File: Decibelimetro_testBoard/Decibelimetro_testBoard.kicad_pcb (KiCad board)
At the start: 2 copper layers, 80 x 65 mm, 16 parts, among them J1 Conn_01x02_Pin, SW1 SW_Push, SW2 SW_Push, U1 ESP32-DEVKITV1-30PIN, U2 INMP441, U3 TFT 1.44" ST7735

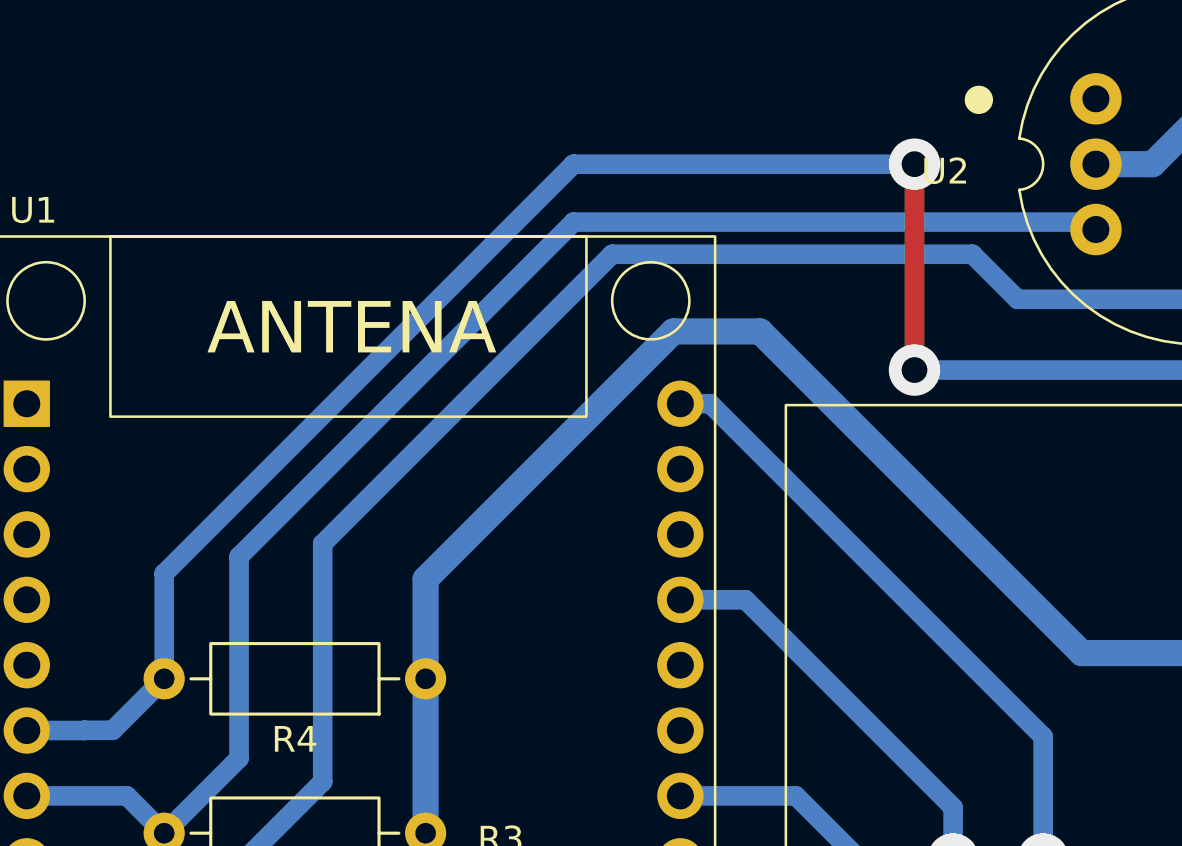
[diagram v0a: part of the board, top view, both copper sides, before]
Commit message: Incorporo cambios de código sonometroV2
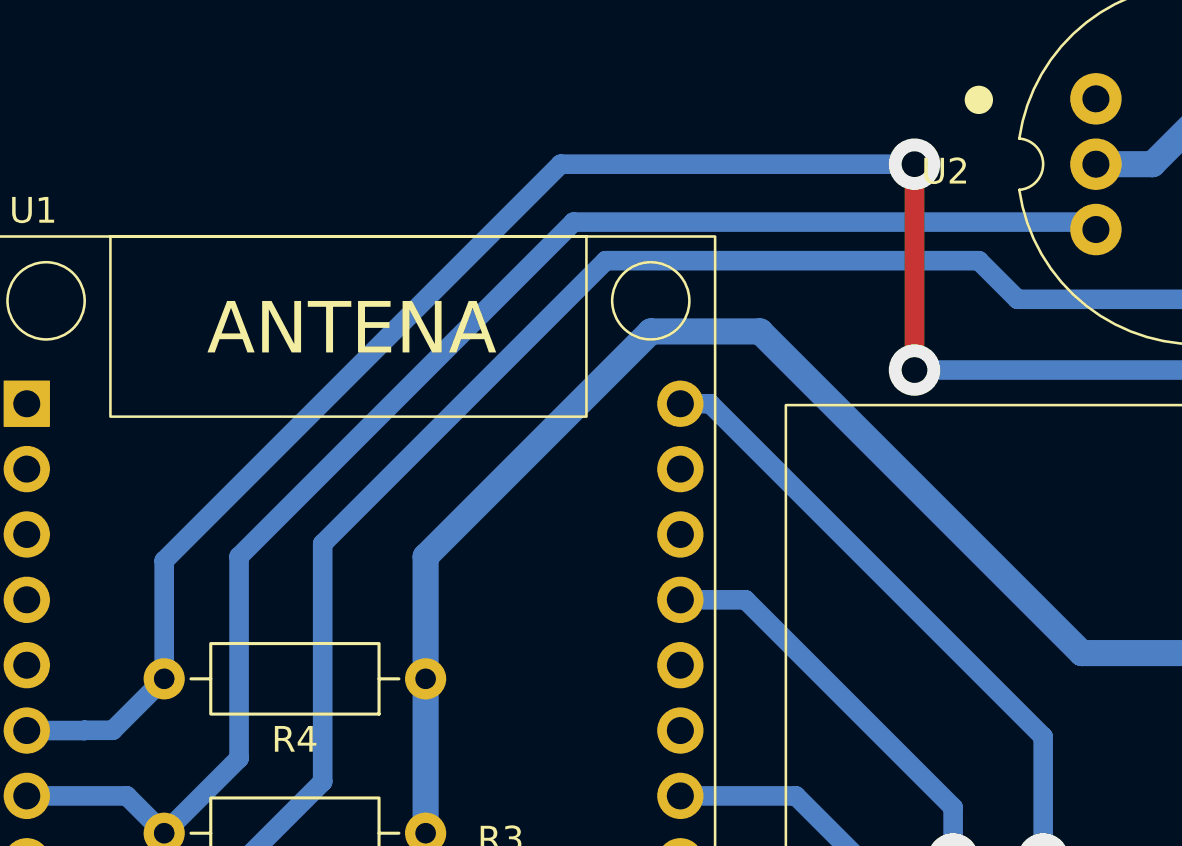
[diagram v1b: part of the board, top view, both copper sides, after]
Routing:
- net +3.3V: track 185.7 -> 186.2 mm
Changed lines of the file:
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@@
 		(tenting front back)
 		(pcbplotparams
-			(layerselection 0x00000000_00000000_55555555_5755f5ff)
-			(plot_on_all_layers_selection 0x00000000_00000000_00000000_00000000)
+			(layerselection 0x00000000_00000000_55555555_55555554)
+			(plot_on_all_layers_selection 0x00000000_00000000_00000000_02000000)
 			(disableapertmacros no)
 			(usegerberextensions no)
@@
 			(pdf_single_document no)
 			(dxfpolygonmode yes)
-			(dxfimperialunits yes)
+			(dxfimperialunits no)
 			(dxfusepcbnewfont yes)
 			(psnegative no)
@@
 			(crossoutdnponfab yes)
 			(subtractmaskfromsilk no)
-			(outputformat 1)
+			(outputformat 3)
 			(mirror no)
-			(drillshape 1)
+			(drillshape 2)
 			(scaleselection 1)
-			(outputdirectory "")
+			(outputdirectory "Fabricacion/")
 		)
 	)
@@
 	)
 	(segment
-		(start 144.625 86.5)
-		(end 148 86.5)
-		(width 1.016)
-		(layer "B.Cu")
-		(net 5)
-	)
-	(segment
 		(start 141.37 124.87)
 		(end 135 118.5)
@@
 	)
 	(segment
-		(start 135 100)
-		(end 135 96.125)
-		(width 1.016)
-		(layer "B.Cu")
-		(net 5)
-	)
-	(segment
 		(start 175 115)
 		(end 177.5 115)
@@
 	)
 	(segment
-		(start 156.1 128.6)
-		(end 155 127.5)
+		(start 135 95.25)
+		(end 143.75 86.5)
 		(width 1.016)
 		(layer "B.Cu")
@@
 	)
 	(segment
-		(start 160.5 99)
-		(end 177.5 99)
+		(start 135 100)
+		(end 135 95.25)
+		(width 1.016)
+		(layer "B.Cu")
+		(net 5)
+	)
+	(segment
+		(start 156.1 128.6)
+		(end 155 127.5)
 		(width 1.016)
 		(layer "B.Cu")
@@
 	)
 	(segment
+		(start 160.5 99)
+		(end 177.5 99)
+		(width 1.016)
+		(layer "B.Cu")
+		(net 5)
+	)
+	(segment
 		(start 177.5 99)
 		(end 177.5 115)
@@
 	)
 	(segment
-		(start 135 96.125)
-		(end 144.625 86.5)
+		(start 155 127.5)
+		(end 152.37 124.87)
 		(width 1.016)
 		(layer "B.Cu")
@@
 	)
 	(segment
-		(start 155 127.5)
-		(end 152.37 124.87)
+		(start 166 75.75)
+		(end 167 74.75)
 		(width 1.016)
 		(layer "B.Cu")
@@
 	)
 	(segment
-		(start 148 86.5)
-		(end 160.5 99)
+		(start 143.75 86.5)
+		(end 148 86.5)
 		(width 1.016)
 		(layer "B.Cu")
@@
 	)
 	(segment
-		(start 166 75.75)
-		(end 167 74.75)
+		(start 135 118.5)
+		(end 135 106)
 		(width 1.016)
 		(layer "B.Cu")
@@
 	)
 	(segment
-		(start 135 118.5)
-		(end 135 106)
+		(start 148 86.5)
+		(end 160.5 99)
 		(width 1.016)
 		(layer "B.Cu")
@@
 	)
 	(segment
-		(start 124.84 95.91)
-		(end 140.75 80)
+		(start 124.84 95.41)
+		(end 140.25 80)
 		(width 0.762)
 		(layer "B.Cu")
@@
 	)
 	(segment
-		(start 140.75 80)
-		(end 154 80)
-		(width 0.762)
-		(layer "B.Cu")
-		(net 7)
-	)
-	(segment
 		(start 124.84 100)
-		(end 124.84 95.91)
+		(end 124.84 95.41)
 		(width 0.762)
 		(layer "B.Cu")
@@
 	)
 	(segment
+		(start 140.25 80)
+		(end 154 80)
+		(width 0.762)
+		(layer "B.Cu")
+		(net 7)
+	)
+	(segment
 		(start 164.84 115)
 		(end 164.84 113.09)
@@
 	)
 	(segment
-		(start 156.25 83.5)
-		(end 158 85.25)
+		(start 126 109)
+		(end 131 104)
 		(width 0.762)
 		(layer "B.Cu")
@@
 	)
 	(segment
-		(start 122.34 107.09)
-		(end 124.25 109)
+		(start 165.25 85.25)
+		(end 165.5 85)
 		(width 0.762)
 		(layer "B.Cu")
@@
 	)
 	(segment
-		(start 165.5 80.75)
-		(end 166.25 80)
+		(start 119.5 107.09)
+		(end 122.34 107.09)
 		(width 0.762)
 		(layer "B.Cu")
@@
 	)
 	(segment
-		(start 131 94.75)
-		(end 142.25 83.5)
+		(start 142 83.75)
+		(end 156.5 83.75)
 		(width 0.762)
 		(layer "B.Cu")
@@
 	)
 	(segment
-		(start 165.25 85.25)
-		(end 165.5 85)
+		(start 165.5 80.75)
+		(end 166.25 80)
 		(width 0.762)
 		(layer "B.Cu")
@@
 	)
 	(segment
-		(start 165.5 85)
-		(end 165.5 80.75)
+		(start 124.25 109)
+		(end 126 109)
 		(width 0.762)
 		(layer "B.Cu")
@@
 	)
 	(segment
-		(start 119.5 107.09)
-		(end 122.34 107.09)
+		(start 165.5 85)
+		(end 165.5 80.75)
 		(width 0.762)
 		(layer "B.Cu")
@@
 	)
 	(segment
-		(start 142.25 83.5)
-		(end 156.25 83.5)
+		(start 166.25 80)
+		(end 168.95 80)
 		(width 0.762)
 		(layer "B.Cu")
@@
 	)
 	(segment
-		(start 126 109)
-		(end 131 104)
+		(start 131 104)
+		(end 131 94.75)
 		(width 0.762)
 		(layer "B.Cu")
@@
 	)
 	(segment
-		(start 166.25 80)
-		(end 168.95 80)
+		(start 156.5 83.75)
+		(end 158 85.25)
 		(width 0.762)
 		(layer "B.Cu")
@@
 	)
 	(segment
-		(start 124.25 109)
-		(end 126 109)
+		(start 122.34 107.09)
+		(end 124.25 109)
 		(width 0.762)
 		(layer "B.Cu")
@@
 	)
 	(segment
-		(start 131 104)
-		(end 131 94.75)
+		(start 131 94.75)
+		(end 142 83.75)
 		(width 0.762)
 		(layer "B.Cu")
@@
 			(thermal_gap 0.5)
 			(thermal_bridge_width 0.5)
+			(island_removal_mode 1)
+			(island_area_min 10)
 		)
 		(polygon
